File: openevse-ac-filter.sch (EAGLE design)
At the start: 8 parts

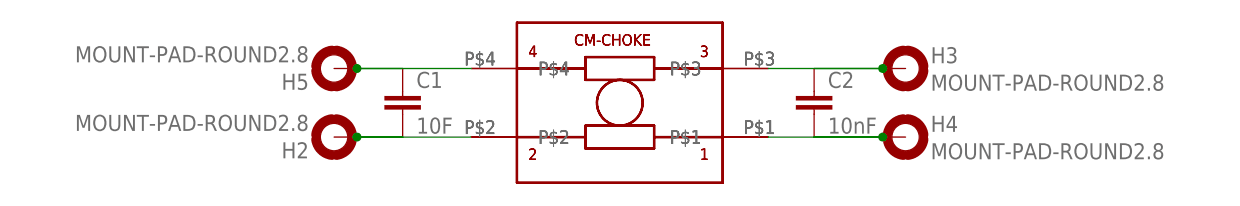
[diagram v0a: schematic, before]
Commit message: V1.2 decrease hole size
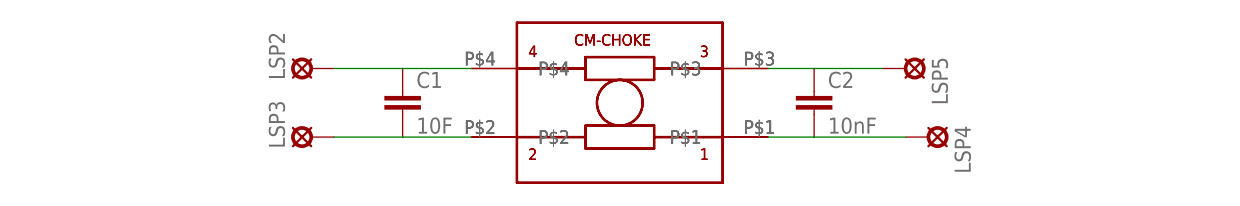
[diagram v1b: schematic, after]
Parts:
- removed H2, H3, H4, H5: MOUNT-PAD-ROUND2.8, holes:MOUNT-PAD-ROUND2.8
- added LSP2, LSP3, LSP4, LSP5: SE13, solpad:SE13
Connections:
- net N$1: now also LSP2.MP; no longer H5.MOUNT
- net N$2: now also LSP3.MP; no longer H2.MOUNT
- net N$3: now also LSP5.MP; no longer H3.MOUNT
- net N$4: now also LSP4.MP; no longer H4.MOUNT
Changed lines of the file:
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@@
 <?xml version="1.0" encoding="utf-8"?>
 <!DOCTYPE eagle SYSTEM "eagle.dtd">
-<eagle version="7.7.0">
+<eagle version="8.3.1">
 <drawing>
 <settings>
 <setting alwaysvectorfont="no"/>
+<setting keepoldvectorfont="yes"/>
 <setting verticaltext="up"/>
 </settings>
@@
 <layer number="91" name="Nets" color="2" fill="1" visible="yes" active="yes"/>
 <layer number="92" name="Busses" color="1" fill="1" visible="yes" active="yes"/>
-<layer number="93" name="Pins" color="2" fill="1" visible="no" active="yes"/>
+<layer number="93" name="Pins" color="2" fill="1" visible="yes" active="yes"/>
 <layer number="94" name="Symbols" color="4" fill="1" visible="yes" active="yes"/>
 <layer number="95" name="Names" color="7" fill="1" visible="yes" active="yes"/>
@@
 <part name="C1" library="capacitor-wima" deviceset="C" device="5/2.5" value="10F"/>
 <part name="C2" library="capacitor-wima" deviceset="C" device="5/2.5" value="10nF"/>
-<part name="H2" library="holes" deviceset="MOUNT-PAD-ROUND" device="2.8"/>
-<part name="H3" library="holes" deviceset="MOUNT-PAD-ROUND" device="2.8"/>
-<part name="H4" library="holes" deviceset="MOUNT-PAD-ROUND" device="2.8"/>
-<part name="H5" library="holes" deviceset="MOUNT-PAD-ROUND" device="2.8"/>
+<part name="LSP2" library="solpad" library_urn="urn:adsk.eagle:library:364" deviceset="SE13" device="" package3d_urn="urn:adsk.eagle:package:26505/1"/>
+<part name="LSP3" library="solpad" library_urn="urn:adsk.eagle:library:364" deviceset="SE13" device="" package3d_urn="urn:adsk.eagle:package:26505/1"/>
+<part name="LSP4" library="solpad" library_urn="urn:adsk.eagle:library:364" deviceset="SE13" device="" package3d_urn="urn:adsk.eagle:package:26505/1"/>
+<part name="LSP5" library="solpad" library_urn="urn:adsk.eagle:library:364" deviceset="SE13" device="" package3d_urn="urn:adsk.eagle:package:26505/1"/>
 </parts>
 <sheets>
@@
 <instance part="C1" gate="G$1" x="10.16" y="73.66"/>
 <instance part="C2" gate="G$1" x="55.88" y="73.66"/>
-<instance part="H2" gate="G$1" x="2.54" y="68.58" rot="R180"/>
-<instance part="H3" gate="G$1" x="66.04" y="76.2"/>
-<instance part="H4" gate="G$1" x="66.04" y="68.58"/>
-<instance part="H5" gate="G$1" x="2.54" y="76.2" rot="R180"/>
+<instance part="LSP2" gate="1" x="0" y="76.2" rot="R90"/>
+<instance part="LSP3" gate="1" x="0" y="68.58" rot="R90"/>
+<instance part="LSP4" gate="1" x="68.58" y="68.58" rot="R270"/>
+<instance part="LSP5" gate="1" x="66.04" y="76.2" rot="R270"/>
 </instances>
 <busses>
@@
 <pinref part="U$2" gate="G$1" pin="P$4"/>
 <pinref part="C1" gate="G$1" pin="1"/>
-<wire x1="17.78" y1="76.2" x2="5.08" y2="76.2" width="0.1524" layer="91"/>
-<pinref part="H5" gate="G$1" pin="MOUNT"/>
-<junction x="5.08" y="76.2"/>
-<wire x1="5.08" y1="76.2" x2="10.16" y2="76.2" width="0.1524" layer="91"/>
+<wire x1="17.78" y1="76.2" x2="10.16" y2="76.2" width="0.1524" layer="91"/>
+<wire x1="2.54" y1="76.2" x2="10.16" y2="76.2" width="0.1524" layer="91"/>
+<pinref part="LSP2" gate="1" pin="MP"/>
 </segment>
 </net>
@@
 <pinref part="U$2" gate="G$1" pin="P$2"/>
 <pinref part="C1" gate="G$1" pin="2"/>
-<wire x1="5.08" y1="68.58" x2="17.78" y2="68.58" width="0.1524" layer="91"/>
-<pinref part="H2" gate="G$1" pin="MOUNT"/>
-<junction x="5.08" y="68.58"/>
-<wire x1="5.08" y1="68.58" x2="10.16" y2="68.58" width="0.1524" layer="91"/>
+<wire x1="10.16" y1="68.58" x2="17.78" y2="68.58" width="0.1524" layer="91"/>
+<wire x1="2.54" y1="68.58" x2="10.16" y2="68.58" width="0.1524" layer="91"/>
+<pinref part="LSP3" gate="1" pin="MP"/>
 </segment>
 </net>
@@
 <pinref part="U$2" gate="G$1" pin="P$3"/>
 <pinref part="C2" gate="G$1" pin="1"/>
-<wire x1="50.8" y1="76.2" x2="63.5" y2="76.2" width="0.1524" layer="91"/>
-<pinref part="H3" gate="G$1" pin="MOUNT"/>
-<junction x="63.5" y="76.2"/>
+<wire x1="50.8" y1="76.2" x2="55.88" y2="76.2" width="0.1524" layer="91"/>
 <wire x1="63.5" y1="76.2" x2="55.88" y2="76.2" width="0.1524" layer="91"/>
+<pinref part="LSP5" gate="1" pin="MP"/>
 </segment>
 </net>
@@
 <pinref part="U$2" gate="G$1" pin="P$1"/>
 <pinref part="C2" gate="G$1" pin="2"/>
-<wire x1="50.8" y1="68.58" x2="63.5" y2="68.58" width="0.1524" layer="91"/>
-<pinref part="H4" gate="G$1" pin="MOUNT"/>
-<junction x="63.5" y="68.58"/>
-<wire x1="63.5" y1="68.58" x2="55.88" y2="68.58" width="0.1524" layer="91"/>
+<wire x1="50.8" y1="68.58" x2="55.88" y2="68.58" width="0.1524" layer="91"/>
+<wire x1="66.04" y1="68.58" x2="55.88" y2="68.58" width="0.1524" layer="91"/>
+<pinref part="LSP4" gate="1" pin="MP"/>
 </segment>
 </net>
@@
 </schematic>
 </drawing>
+<compatibility>
+<note version="8.2" severity="warning">
+Since Version 8.2, EAGLE supports online libraries. The ids
+of those online libraries will not be understood (or retained)
+with this version.
+</note>
+<note version="8.3" severity="warning">
+Since Version 8.3, EAGLE supports URNs for individual library
+assets (packages, symbols, and devices). The URNs of those assets
+will not be understood (or retained) with this version.
+</note>
+<note version="8.3" severity="warning">
+Since Version 8.3, EAGLE supports the association of 3D packages
+with devices in libraries, schematics, and board files. Those 3D
+packages will not be understood (or retained) with this version.
+</note>
+</compatibility>
 </eagle>
